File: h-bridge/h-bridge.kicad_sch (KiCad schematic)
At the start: 32 parts, among them Q1 IRF4905, Q2 IRLZ44N, Q3 IRF4905, Q4 IRLZ44N, Q5 2N2222, Q6 2N2222, Q7 IRF4905, Q8 IRF4905

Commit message: Updated BOM
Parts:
- removed D11, D12, D13, D14, D5, D6, D7, D8: 1N4148, Diode_THT:D_DO-35_SOD27_P7.62mm_Horizontal, symbol Diode:1N4148
- removed R2, R3, R5, R6: 1k, symbol Device:R_US
- added D10, D15, D16, D9: 1N4148, Diode_THT:D_DO-35_SOD27_P7.62mm_Horizontal, symbol Diode:1N4148
- added R13, R14: 1k, symbol Device:R_US
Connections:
- net GND: now also D10.2 (A), D16.2 (A), R13.2, R14.2
- net VCC: now also D15.1 (K), D9.1 (K)
- net Vf: now also D9.2 (A), R13.1
- net Vr: now also D15.2 (A), R14.1
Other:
- moved on the sheet: D1, D2, D3, D4, Q1, Q2, Q3, Q4, Q5, Q6, Q7, Q8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

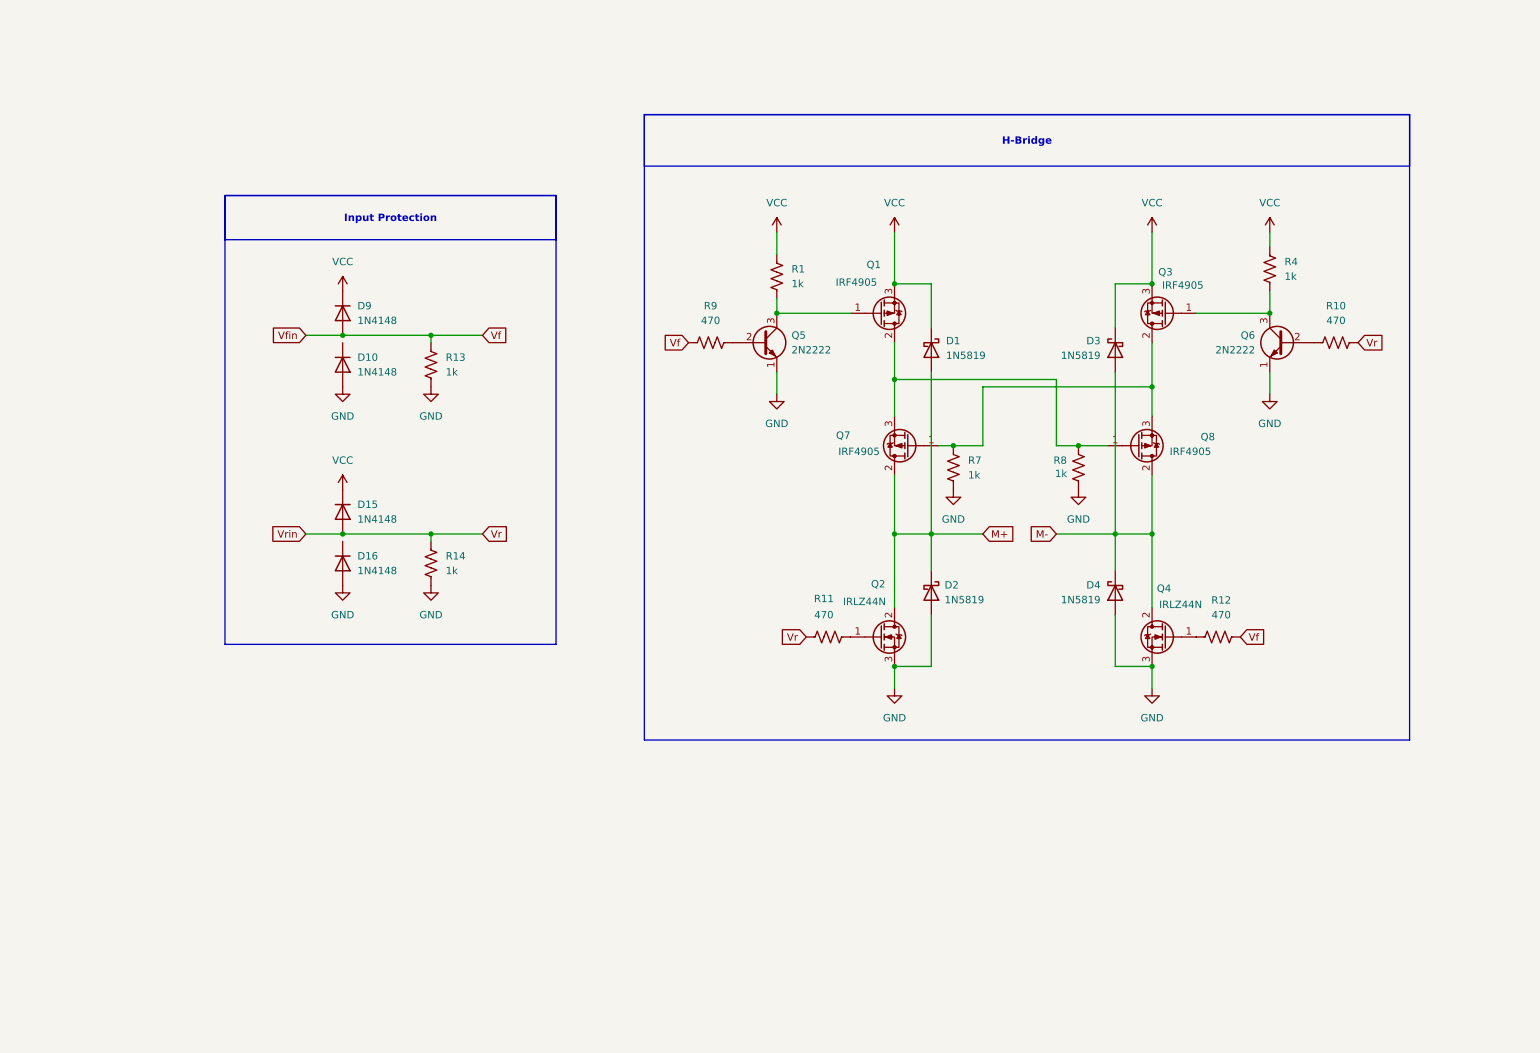
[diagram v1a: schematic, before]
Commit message: Added screw terminal
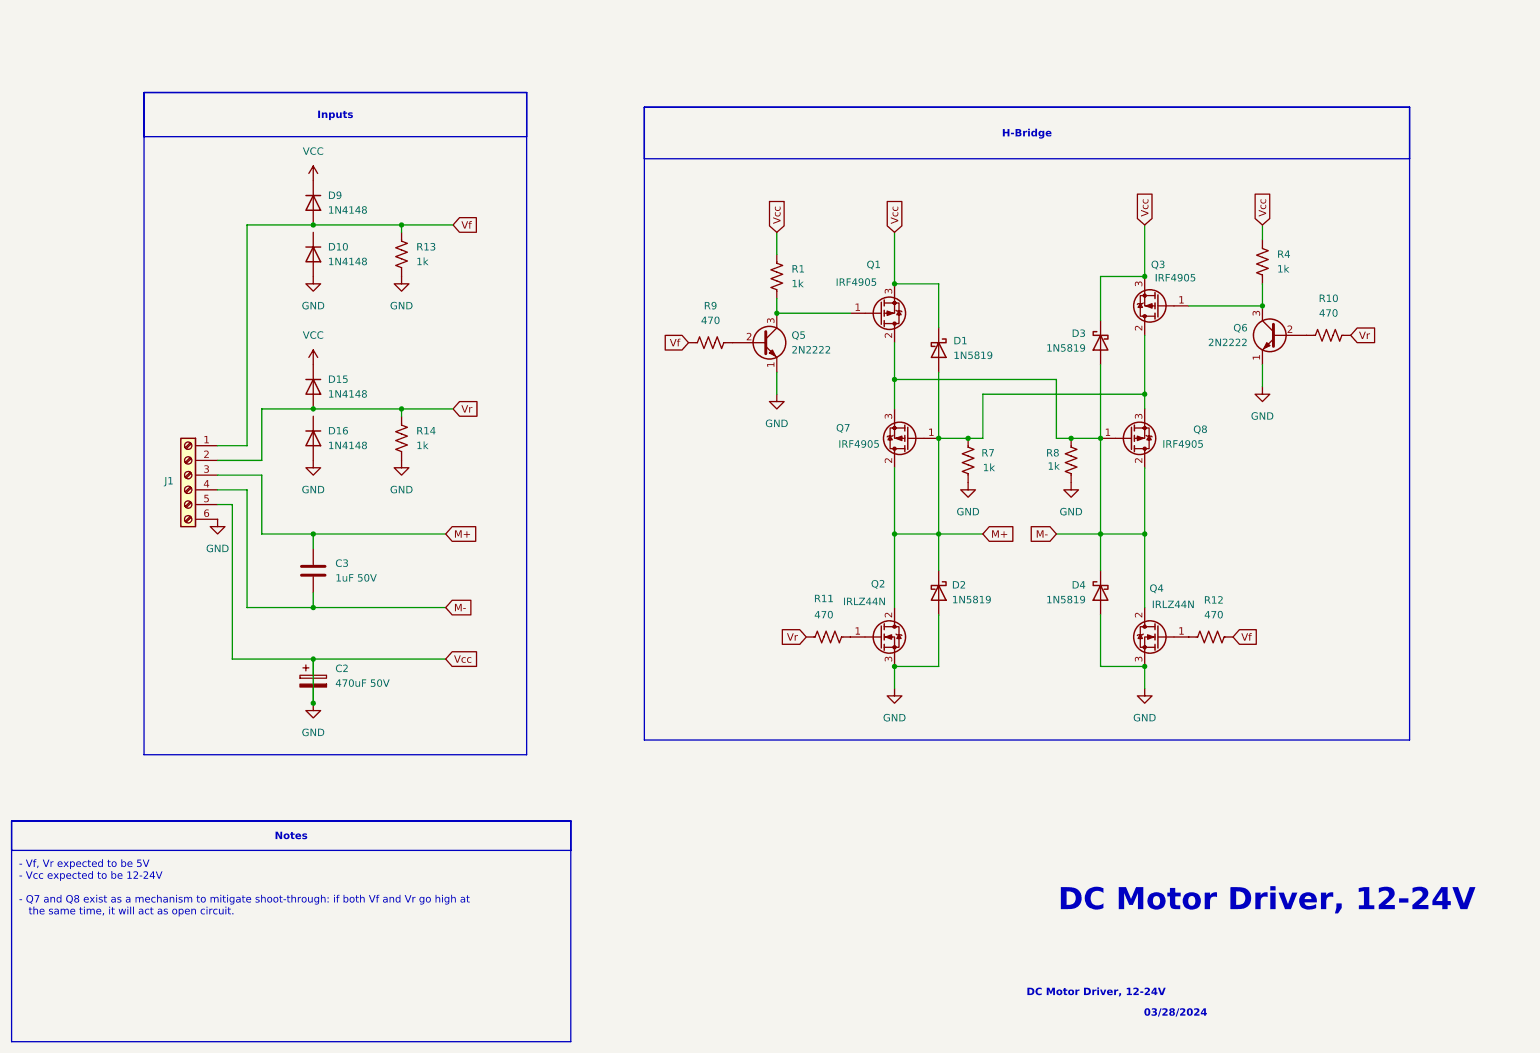
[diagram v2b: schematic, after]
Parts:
- added C2: 470uF 50V, Capacitor_THT:CP_Radial_D8.0mm_P3.80mm, symbol Device:C_Polarized
- added C3: 1uF 50V, Capacitor_THT:C_Disc_D5.0mm_W2.5mm_P5.00mm, symbol Device:C
- added J1: Screw_Terminal_01x06, symbol Connector:Screw_Terminal_01x06
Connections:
- net GND: now also D1.1 (K), D3.1 (K), Q1.3 (S), Q3.3 (S), R1.1, R4.1, C2.1, C2.2, J1.5 (Pin_5), J1.6 (Pin_6)
- net M+: now also Q3.2 (D), Q7.1 (G), Q8.3 (S), R7.1, C3.1, J1.3 (Pin_3)
- net M-: now also Q1.2 (D), Q7.3 (S), Q8.1 (G), R8.1, C3.2, J1.4 (Pin_4)
- net VCC: no longer D1.1 (K), D3.1 (K), Q1.3 (S), Q3.3 (S), R1.1, R4.1
- net Vf: now also J1.1 (Pin_1)
- net Vr: now also J1.2 (Pin_2)
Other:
- note added: "- Vf, Vr expected to be 5V - Vcc expected to be 12-24V - Q7 and Q8 exist as a mechanism to mitigate shoot-through: if both Vf and Vr go high at the same time, it will act as open circuit."
- note added: "03/28/2024"
- note added: "DC Motor Driver, 12-24V"
- moved on the sheet: D1, D10, D15, D16, D2, D3, D4, D9, Q3, Q4, Q6, Q7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

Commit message: pcb layed out
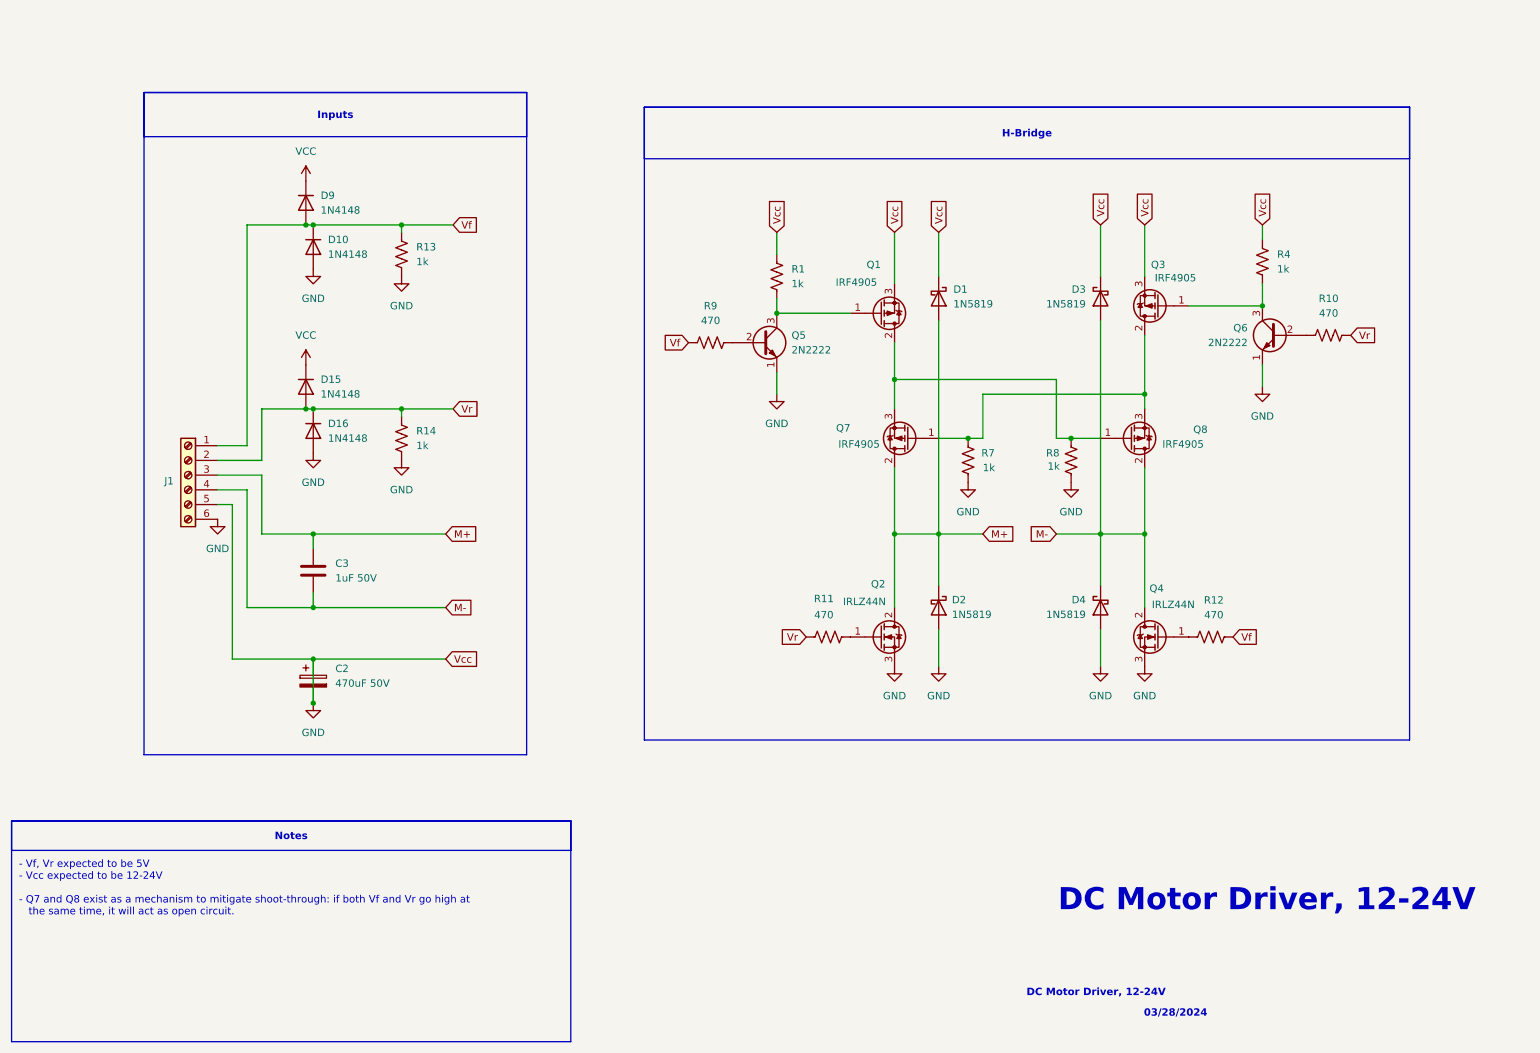
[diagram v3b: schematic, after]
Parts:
- J1: footprint (none) -> TerminalBlock:TerminalBlock_Xinya_XY308-2.54-6P_1x06_P2.54mm_Horizontal
- Q5, Q6: footprint Package_TO_SOT_THT:TO-39-3 -> Package_TO_SOT_THT:TO-92_Inline_Horizontal1
- R1, R10, R11, R12, R13, R14, R4, R7, R8, R9: footprint (none) -> Resistor_THT:R_Axial_DIN0207_L6.3mm_D2.5mm_P10.16mm_Horizontal
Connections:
- net M+: no longer Q3.2 (D), Q7.1 (G), Q8.3 (S), R7.1
- net M-: no longer Q1.2 (D), Q7.3 (S), Q8.1 (G), R8.1
- net Vf: now also D10.1 (K)
- net Vr: now also D16.1 (K)
- new net: Q3.2 (D), Q7.1 (G), Q8.3 (S), R7.1
- new net: Q1.2 (D), Q7.3 (S), Q8.1 (G), R8.1
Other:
- moved on the sheet: D1, D10, D15, D16, D2, D3, D4, D9

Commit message: V2 Redesign Submitted to JLCPCB and BOM generated
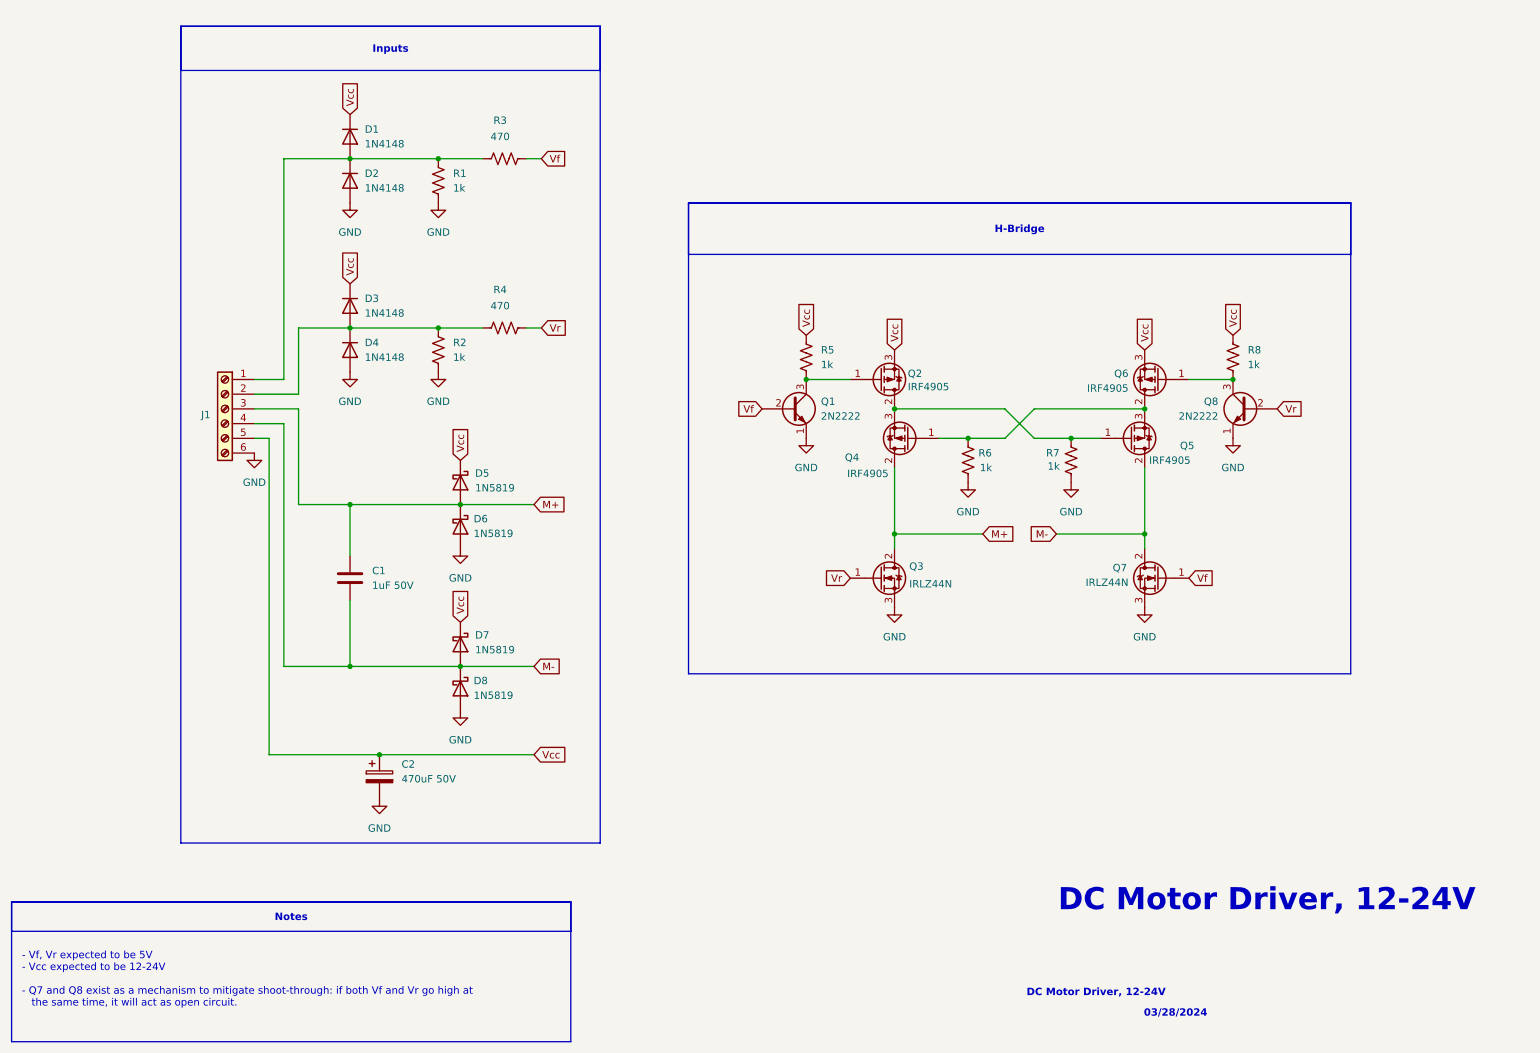
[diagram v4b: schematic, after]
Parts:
- removed D1, D2, D3, D4: 1N5819, Diode_THT:D_DO-41_SOD81_P10.16mm_Horizontal, symbol Diode:1N5819
- removed D16: 1N4148, Diode_THT:D_DO-35_SOD27_P7.62mm_Horizontal, symbol Diode:1N4148
- removed R10, R11, R12, R9: 470, Resistor_THT:R_Axial_DIN0207_L6.3mm_D2.5mm_P10.16mm_Horizontal, symbol Device:R_US
- added D4: 1N4148, Diode_THT:D_DO-35_SOD27_P7.62mm_Horizontal, symbol Diode:1N4148
- added D5, D6, D7, D8: 1N5819, Diode_THT:D_DO-41_SOD81_P10.16mm_Horizontal, symbol Diode:1N5819
- added R3, R4: 470, Resistor_THT:R_Axial_DIN0207_L6.3mm_D2.5mm_P10.16mm_Horizontal, symbol Device:R_US
- renumbered C3 to C1, D9 to D1, D10 to D2, D15 to D3, Q5 to Q1, Q1 to Q2, Q2 to Q3, Q7 to Q4, Q8 to Q5, Q3 to Q6, Q4 to Q7, Q6 to Q8, R13 to R1, R14 to R2, R1 to R5, R7 to R6, R8 to R7, R4 to R8
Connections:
- net GND: now also D4.2 (A), D6.2 (A), D8.2 (A); no longer C2.1, J1.5 (Pin_5), Q2.3 (S), Q6.3 (S), R5.1, R8.1
- net M+: now also D5.2 (A), D6.1 (K)
- net M-: now also D7.2 (A), D8.1 (K)
- net Vf: now also Q1.2 (B), Q7.1 (G), R3.2; no longer D1.2 (A), D2.1 (K), J1.1 (Pin_1), R1.1
- net Vr: now also Q3.1 (G), Q8.2 (B), R4.2; no longer D3.2 (A), J1.2 (Pin_2), R2.1
- net VCC renamed Vcc
- net Vcc: now also C2.1, J1.5 (Pin_5), Q2.3 (S), Q6.3 (S), R5.1, R8.1, D5.1 (K), D7.1 (K)
- new net: D3.2 (A), D4.1 (K), J1.2 (Pin_2), R2.1, R4.1
- new net: D1.2 (A), D2.1 (K), J1.1 (Pin_1), R1.1, R3.1
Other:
- moved on the sheet: C1, C2, D1, D2, D3, J1, Q1, Q2, Q3, Q6, Q7, Q8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

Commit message: V3 submitted to JLCPCB
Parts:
- Q1, Q8: footprint Package_TO_SOT_THT:TO-92_Inline_Horizontal1 -> Package_TO_SOT_THT:TO-92_HandSolder
- Q2, Q4, Q5, Q6: value IRF4905 -> FQP27P06
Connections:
- net Vf: now also D1.2 (A), D2.1 (K), J1.1 (Pin_1), R1.1, R3.1; no longer Q1.2 (B), R3.2
- net Vr: now also D3.2 (A), D4.1 (K), J1.2 (Pin_2), R2.1; no longer Q8.2 (B)
- new net: Q8.2 (B), R4.1
- new net: Q1.2 (B), R3.2
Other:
- note added: "- Vf, Vr expected to be 5V - Vcc expected to be 12-24V - Q4 and Q5 exist as a mechanism to mitigate shoot-through: if both Vf and Vr go high at the same time, it will act as open circuit."
- note removed: "- Vf, Vr expected to be 5V - Vcc expected to be 12-24V - Q7 and Q8 exist as a mechanism to mitigate shoot-through: if both Vf and Vr go high at the same time, it will act as open circuit."
- moved on the sheet: D1, D2, D3, D4, R1, R2, R3, R4
